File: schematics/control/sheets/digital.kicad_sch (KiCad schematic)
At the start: 22 parts, among them U1 Pico, U3 TL072, U4 CD4051B, U5 MCP4822

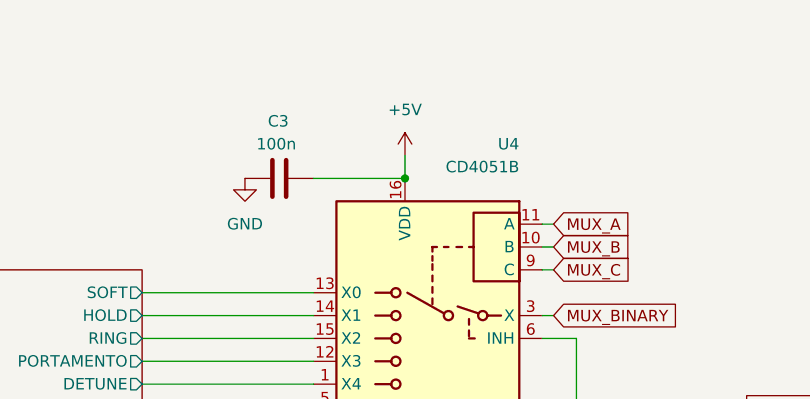
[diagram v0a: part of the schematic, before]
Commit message: Updated MUX reading
For some reason I couldn't figure out yet, there was one step offset
in the reading of the multiplexer input. :/ Now it works as intended
but it's still annoying.
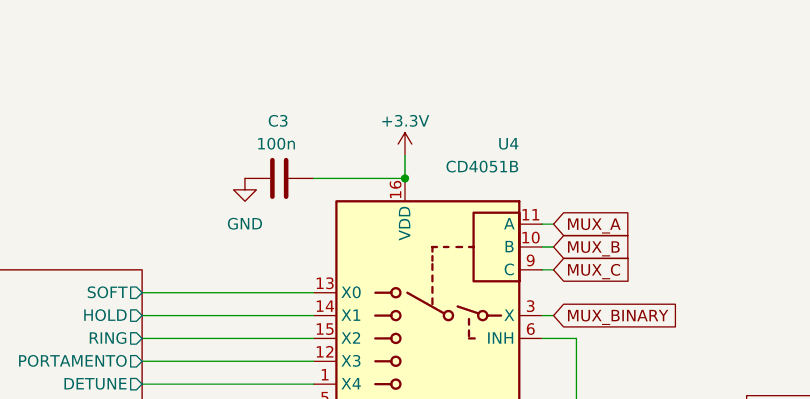
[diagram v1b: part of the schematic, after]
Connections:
- net +3.3V: now also C3.1, U4.16 (VDD)
- net +5V: no longer C3.1, U4.16 (VDD)
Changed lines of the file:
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@@
+    )
+  )
+  (symbol (lib_name "+3.3V_1") (lib_id "power:+3.3V") (at 157.48 36.83 0) (mirror y) (unit 1)
+    (in_bom yes) (on_board yes) (dnp no)
+    (property "Reference" "#PWR011" (at 157.48 40.64 0)
+      (effects (font (size 1.27 1.27)) hide)
+    )
+    (property "Value" "+3.3V" (at 157.48 33.02 0)
+      (effects (font (size 1.27 1.27)))
+    )
+    (property "Footprint" "" (at 157.48 36.83 0)
+      (effects (font (size 1.27 1.27)) hide)
+    )
+    (property "Datasheet" "" (at 157.48 36.83 0)
+      (effects (font (size 1.27 1.27)) hide)
+    )
+    (pin "1")
+    (instances
+      (project "shmoergh-funk-live-control"
+        (path "/6d7b782d-8b2e-4b40-a99f-4bf41187d978/88d90181-522e-4756-bb1e-20cf1e1feb05"
+          (reference "#PWR011") (unit 1)
+        )
+      )
     )
   )
@@
         )
       )
-    )
-  )
-  (symbol (lib_id "power:+5V") (at 157.48 36.83 0) (mirror y) (unit 1)
-    (in_bom yes) (on_board yes) (dnp no) (fields_autoplaced)
-    (property "Reference" "#PWR011" (at 157.48 40.64 0)
-      (effects (font (size 1.27 1.27)) hide)
-    )
-    (property "Value" "+5V" (at 157.48 31.75 0)
-      (effects (font (size 1.27 1.27)))
-    )
-    (property "Footprint" "" (at 157.48 36.83 0)
-      (effects (font (size 1.27 1.27)) hide)
-    )
-    (property "Datasheet" "" (at 157.48 36.83 0)
-      (effects (font (size 1.27 1.27)) hide)
-    )
-    (pin "1")
-    (instances
-      (project "shmoergh-funk-live-control"
-        (path "/6d7b782d-8b2e-4b40-a99f-4bf41187d978/88d90181-522e-4756-bb1e-20cf1e1feb05"
-          (reference "#PWR011") (unit 1)
-        )
-      )
-      (project "rooster"
-        (path "/b5747119-8466-4610-a9a6-85ad63a1d16b"
-          (reference "#PWR?") (unit 1)
-        )
-      )

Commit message: Schemo work
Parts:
- C1, C2, C3: footprint (none) -> Capacitor_THT:C_Disc_D3.0mm_W2.0mm_P2.50mm
- D1: footprint (none) -> Diode_THT:D_DO-35_SOD27_P7.62mm_Horizontal
- J_MIDI_IN?: footprint (none) -> Shmoergh_Custom_Footprints:NSL25_01x02_Vertical
- J_SWD_IO1: footprint (none) -> Shmoergh_Custom_Footprints:NSL25_01x04_Vertical
- R4, R5, R6, R7, R? (x3): footprint (none) -> Shmoergh_Custom_Footprints:R_Axial_DIN0207_L6.3mm_D2.5mm_P7.62mm_Horizontal
- RV_ENV_GAIN1: footprint (none) -> Potentiometer_THT:Potentiometer_Runtron_RM-065_Vertical
- TP_ENV_OUT1, TP_FILT_MOD1: footprint (none) -> TestPoint:TestPoint_THTPad_D2.0mm_Drill1.0mm
- U1: footprint (none) -> MCU_RaspberryPi_and_Boards:RPi_Pico_SMD_TH
- U3, U5, U?: footprint (none) -> PCM_Package_DIP_AKL:DIP-8_W7.62mm_LongPads
- U4: footprint (none) -> PCM_Package_DIP_AKL:DIP-16_W7.62mm_LongPads
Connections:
- net AMP_1: now also U1.27 (GPIO21); no longer U1.21 (GPIO16)
- net AMP_2: now also U1.26 (GPIO20); no longer U1.22 (GPIO17)
- net AMP_3: now also U1.25 (GPIO19); no longer U1.24 (GPIO18)
- net AMP_4: now also U1.24 (GPIO18); no longer U1.25 (GPIO19)
- net AMP_5: now also U1.22 (GPIO17); no longer U1.26 (GPIO20)
- net AMP_6: now also U1.21 (GPIO16); no longer U1.27 (GPIO21)
- net Digital UI/EXTRA_GPIO2: now reaches U1.29 (GPIO22)
- net Digital UI/EXTRA_GPIO1: now reaches U1.34 (GPIO28_ADC2)
- no-connect marks 15 -> 13
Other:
- sheet Digital UI ports: added EXTRA_GPIO1, EXTRA_GPIO2; removed none
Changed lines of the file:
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@@
   (junction (at 274.32 74.93) (diameter 0) (color 0 0 0 0)
   )
-  (no_connect (at 73.66 59.69))
   (no_connect (at 33.02 162.56))
   (no_connect (at 25.4 157.48))
@@
   (no_connect (at 58.42 85.09))
   (no_connect (at 73.66 39.37))
-  (no_connect (at 73.66 46.99))
   (no_connect (at 55.88 85.09))
   (wire (pts (xy 88.9 165.1) (xy 95.25 165.1))
@@
     (stroke (width 0) (type default))
   )
+  (wire (pts (xy 92.71 57.15) (xy 95.25 57.15))
+    (stroke (width 0) (type default))
+  )
   (wire (pts (xy 31.75 72.39) (xy 38.1 72.39))
     (stroke (width 0) (type default))
@@
     (stroke (width 0) (type default))
   )
+  (wire (pts (xy 73.66 59.69) (xy 95.25 59.69))
+    (stroke (width 0) (type default))
+  )
   (wire (pts (xy 73.66 172.72) (xy 69.85 172.72))
     (stroke (width 0) (type default))
@@
     (stroke (width 0) (type default))
   )
+  (wire (pts (xy 92.71 46.99) (xy 92.71 57.15))
+    (stroke (width 0) (type default))
+  )
   (wire (pts (xy 31.75 69.85) (xy 38.1 69.85))
     (stroke (width 0) (type default))
@@
   )
   (wire (pts (xy 267.97 86.36) (xy 274.32 86.36))
+    (stroke (width 0) (type default))
+  )
+  (wire (pts (xy 73.66 46.99) (xy 92.71 46.99))
     (stroke (width 0) (type default))
   )
@@
     (effects (font (size 1.27 1.27)) (justify left))
   )
-  (hierarchical_label "AMP_2" (shape output) (at 80.01 77.47 0) (fields_autoplaced)
+  (hierarchical_label "AMP_2" (shape output) (at 80.01 67.31 0) (fields_autoplaced)
     (effects (font (size 1.27 1.27)) (justify left))
   )
@@
     (effects (font (size 1.27 1.27)) (justify right))
   )
-  (hierarchical_label "AMP_3" (shape output) (at 80.01 72.39 0) (fields_autoplaced)
+  (hierarchical_label "AMP_3" (shape output) (at 80.01 69.85 0) (fields_autoplaced)
     (effects (font (size 1.27 1.27)) (justify left))
   )
@@
     (effects (font (size 1.27 1.27)) (justify left))
   )
-  (hierarchical_label "AMP_1" (shape output) (at 80.01 80.01 0) (fields_autoplaced)
+  (hierarchical_label "AMP_1" (shape output) (at 80.01 64.77 0) (fields_autoplaced)
     (effects (font (size 1.27 1.27)) (justify left))
   )
@@
     (effects (font (size 1.27 1.27)) (justify right))
   )
-  (hierarchical_label "AMP_6" (shape output) (at 80.01 64.77 0) (fields_autoplaced)
+  (hierarchical_label "AMP_6" (shape output) (at 80.01 80.01 0) (fields_autoplaced)
     (effects (font (size 1.27 1.27)) (justify left))
   )
-  (hierarchical_label "AMP_4" (shape output) (at 80.01 69.85 0) (fields_autoplaced)
+  (hierarchical_label "AMP_4" (shape output) (at 80.01 72.39 0) (fields_autoplaced)
     (effects (font (size 1.27 1.27)) (justify left))
   )
@@
     (effects (font (size 1.27 1.27)) (justify right))
   )
-  (hierarchical_label "AMP_5" (shape output) (at 80.01 67.31 0) (fields_autoplaced)
+  (hierarchical_label "AMP_5" (shape output) (at 80.01 77.47 0) (fields_autoplaced)
     (effects (font (size 1.27 1.27)) (justify left))
   )
@@
       (effects (font (size 1.27 1.27)) (justify left))
     )
-    (property "Footprint" "" (at 243.84 74.93 0)
+    (property "Footprint" "PCM_Package_DIP_AKL:DIP-8_W7.62mm_LongPads" (at 243.84 74.93 0)
       (effects (font (size 1.27 1.27)) hide)
     )
@@
       (effects (font (size 1.27 1.27)) (justify left))
     )
-    (property "Footprint" "" (at 279.4 72.39 0)
+    (property "Footprint" "TestPoint:TestPoint_THTPad_D2.0mm_Drill1.0mm" (at 279.4 72.39 0)
       (effects (font (size 1.27 1.27)) hide)
     )
@@
       (effects (font (size 1.27 1.27)) (justify left))
     )
-    (property "Footprint" "" (at 57.15 172.72 0)
+    (property "Footprint" "Diode_THT:D_DO-35_SOD27_P7.62mm_Horizontal" (at 57.15 172.72 0)
       (effects (font (size 1.27 1.27)) hide)
     )
@@
       (effects (font (size 1.27 1.27)))
     )
-    (property "Footprint" "" (at 55.88 55.88 90)
+    (property "Footprint" "MCU_RaspberryPi_and_Boards:RPi_Pico_SMD_TH" (at 55.88 55.88 90)
       (effects (font (size 1.27 1.27)) hide)
     )
@@
       (effects (font (size 1.27 1.27)))
     )
-    (property "Footprint" "" (at 264.16 50.038 90)
+    (property "Footprint" "Shmoergh_Custom_Footprints:R_Axial_DIN0207_L6.3mm_D2.5mm_P7.62mm_Horizontal" (at 264.16 50.038 90)
       (effects (font (size 1.27 1.27)) hide)
     )
@@
       (effects (font (size 1.27 1.27)) (justify left))
     )
-    (property "Footprint" "" (at 139.7 38.4048 0)
+    (property "Footprint" "Capacitor_THT:C_Disc_D3.0mm_W2.0mm_P2.50mm" (at 139.7 38.4048 0)
       (effects (font (size 1.27 1.27)) hide)
     )
@@
       (effects (font (size 1.27 1.27)))
     )
-    (property "Footprint" "" (at 264.16 36.83 0)
+    (property "Footprint" "PCM_Package_DIP_AKL:DIP-8_W7.62mm_LongPads" (at 264.16 36.83 0)
       (effects (font (size 1.27 1.27)) hide)
     )
@@
       (effects (font (size 1.27 1.27)) (justify left))
     )
-    (property "Footprint" "" (at 151.13 170.18 0)
+    (property "Footprint" "PCM_Package_DIP_AKL:DIP-8_W7.62mm_LongPads" (at 151.13 170.18 0)
       (effects (font (size 1.27 1.27)) hide)
     )
@@
       (effects (font (size 1.27 1.27)) (justify left))
     )
-    (property "Footprint" "" (at 138.1252 177.8 0)
+    (property "Footprint" "Capacitor_THT:C_Disc_D3.0mm_W2.0mm_P2.50mm" (at 138.1252 177.8 0)
       (effects (font (size 1.27 1.27)) hide)
     )
@@
       (effects (font (size 1.27 1.27)) (justify left))
     )
-    (property "Footprint" "" (at 102.362 167.64 90)
+    (property "Footprint" "Shmoergh_Custom_Footprints:R_Axial_DIN0207_L6.3mm_D2.5mm_P7.62mm_Horizontal" (at 102.362 167.64 90)
       (effects (font (size 1.27 1.27)) hide)
     )
@@
       (effects (font (size 1.27 1.27)) (justify left))
     )
-    (property "Footprint" "" (at 94.742 180.34 90)
+    (property "Footprint" "Shmoergh_Custom_Footprints:R_Axial_DIN0207_L6.3mm_D2.5mm_P7.62mm_Horizontal" (at 94.742 180.34 90)
       (effects (font (size 1.27 1.27)) hide)
     )
@@
       (effects (font (size 1.27 1.27)) (justify left))
     )
-    (property "Footprint" "" (at 34.29 185.42 0)
+    (property "Footprint" "Shmoergh_Custom_Footprints:NSL25_01x02_Vertical" (at 34.29 185.42 0)
       (effects (font (size 1.27 1.27)) hide)
     )
@@
       (effects (font (size 1.27 1.27)) (justify left))
     )
-    (property "Footprint" "" (at 138.1252 170.18 0)
+    (property "Footprint" "Capacitor_THT:C_Disc_D3.0mm_W2.0mm_P2.50mm" (at 138.1252 170.18 0)
       (effects (font (size 1.27 1.27)) hide)
     )
@@
       (effects (font (size 1.27 1.27)))
     )
-    (property "Footprint" "" (at 88.646 177.8 0)
+    (property "Footprint" "PCM_Package_DIP_AKL:DIP-8_W7.62mm_LongPads" (at 88.646 177.8 0)
       (effects (font (size 1.27 1.27)) hide)
     )
@@
       (effects (font (size 1.27 1.27)) (justify left))
     )
-    (property "Footprint" "" (at 252.222 54.61 90)
+    (property "Footprint" "Shmoergh_Custom_Footprints:R_Axial_DIN0207_L6.3mm_D2.5mm_P7.62mm_Horizontal" (at 252.222 54.61 90)
       (effects (font (size 1.27 1.27)) hide)
     )
@@
       (effects (font (size 1.27 1.27)) (justify left))
     )
-    (property "Footprint" "" (at 252.222 92.71 90)
+    (property "Footprint" "Shmoergh_Custom_Footprints:R_Axial_DIN0207_L6.3mm_D2.5mm_P7.62mm_Horizontal" (at 252.222 92.71 90)
       (effects (font (size 1.27 1.27)) hide)
     )
@@
       (effects (font (size 1.27 1.27)) (justify left))
     )
-    (property "Footprint" "" (at 156.21 76.2 0)
+    (property "Footprint" "PCM_Package_DIP_AKL:DIP-16_W7.62mm_LongPads" (at 156.21 76.2 0)
       (effects (font (size 1.27 1.27)) (justify left) hide)
     )
@@
       (effects (font (size 1.27 1.27)))
     )
-    (property "Footprint" "" (at 264.16 88.138 90)
+    (property "Footprint" "Shmoergh_Custom_Footprints:R_Axial_DIN0207_L6.3mm_D2.5mm_P7.62mm_Horizontal" (at 264.16 88.138 90)
       (effects (font (size 1.27 1.27)) hide)
     )
@@
       (effects (font (size 1.27 1.27)))
     )
-    (property "Footprint" "" (at 49.53 169.418 90)
+    (property "Footprint" "Shmoergh_Custom_Footprints:R_Axial_DIN0207_L6.3mm_D2.5mm_P7.62mm_Horizontal" (at 49.53 169.418 90)
       (effects (font (size 1.27 1.27)) hide)
     )
@@
       (effects (font (size 1.27 1.27)))
     )
-    (property "Footprint" "" (at 177.8 170.18 0)
+    (property "Footprint" "Shmoergh_Custom_Footprints:NSL25_01x04_Vertical" (at 177.8 170.18 0)
       (effects (font (size 1.27 1.27)) hide)
     )
@@
       (effects (font (size 1.27 1.27)) (justify right))
     )
-    (property "Footprint" "" (at 274.32 41.91 0)
+    (property "Footprint" "Potentiometer_THT:Potentiometer_Runtron_RM-065_Vertical" (at 274.32 41.91 0)
       (effects (font (size 1.27 1.27)) hide)
     )
@@
       (effects (font (size 1.27 1.27)))
     )
-    (property "Footprint" "" (at 264.16 74.93 0)
+    (property "Footprint" "PCM_Package_DIP_AKL:DIP-8_W7.62mm_LongPads" (at 264.16 74.93 0)
       (effects (font (size 1.27 1.27)) hide)
     )
@@
       (effects (font (size 1.27 1.27)) (justify left))
     )
-    (property "Footprint" "" (at 279.4 34.29 0)
+    (property "Footprint" "TestPoint:TestPoint_THTPad_D2.0mm_Drill1.0mm" (at 279.4 34.29 0)
       (effects (font (size 1.27 1.27)) hide)
     )
@@
       (effects (font (size 1.27 1.27)) (justify right))
     )
-    (instances
+    (pin "EXTRA_GPIO2" output (at 95.25 59.69 180)
+      (effects (font (size 1.27 1.27)) (justify left))
+    )
+    (pin "EXTRA_GPIO1" output (at 95.25 57.15 180)
+      (effects (font (size 1.27 1.27)) (justify left))
+    )
+    (instances

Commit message: Updated schem. + added JLCPCB gerbers
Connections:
- net MUX_A: now also U1.6 (GPIO4); no longer U1.4 (GPIO2)
- net MUX_C: now also U1.4 (GPIO2); no longer U1.6 (GPIO4)
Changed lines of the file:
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@@
     )
   )
-  (global_label "MUX_A" (shape input) (at 31.75 39.37 180) (fields_autoplaced)
+  (global_label "MUX_A" (shape input) (at 31.75 44.45 180) (fields_autoplaced)
     (effects (font (size 1.27 1.27)) (justify right))
-    (property "Intersheetrefs" "${INTERSHEET_REFS}" (at 23.2893 39.2906 0)
+    (property "Intersheetrefs" "${INTERSHEET_REFS}" (at 23.2893 44.3706 0)
       (effects (font (size 1.27 1.27)) (justify right) hide)
     )
   )
-  (global_label "MUX_C" (shape input) (at 31.75 44.45 180) (fields_autoplaced)
+  (global_label "MUX_C" (shape input) (at 31.75 39.37 180) (fields_autoplaced)
     (effects (font (size 1.27 1.27)) (justify right))
-    (property "Intersheetrefs" "${INTERSHEET_REFS}" (at 23.1079 44.3706 0)
+    (property "Intersheetrefs" "${INTERSHEET_REFS}" (at 23.1079 39.2906 0)
       (effects (font (size 1.27 1.27)) (justify right) hide)
     )
